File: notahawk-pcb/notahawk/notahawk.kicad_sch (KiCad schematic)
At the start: 33 parts, among them J1 Conn_01x02_Pin, U2 BNO085, U3 BMP581, U4 ADXL372BCCZ-RL7, U5 W25Q128JVSIQ, U6 ESP32-C3

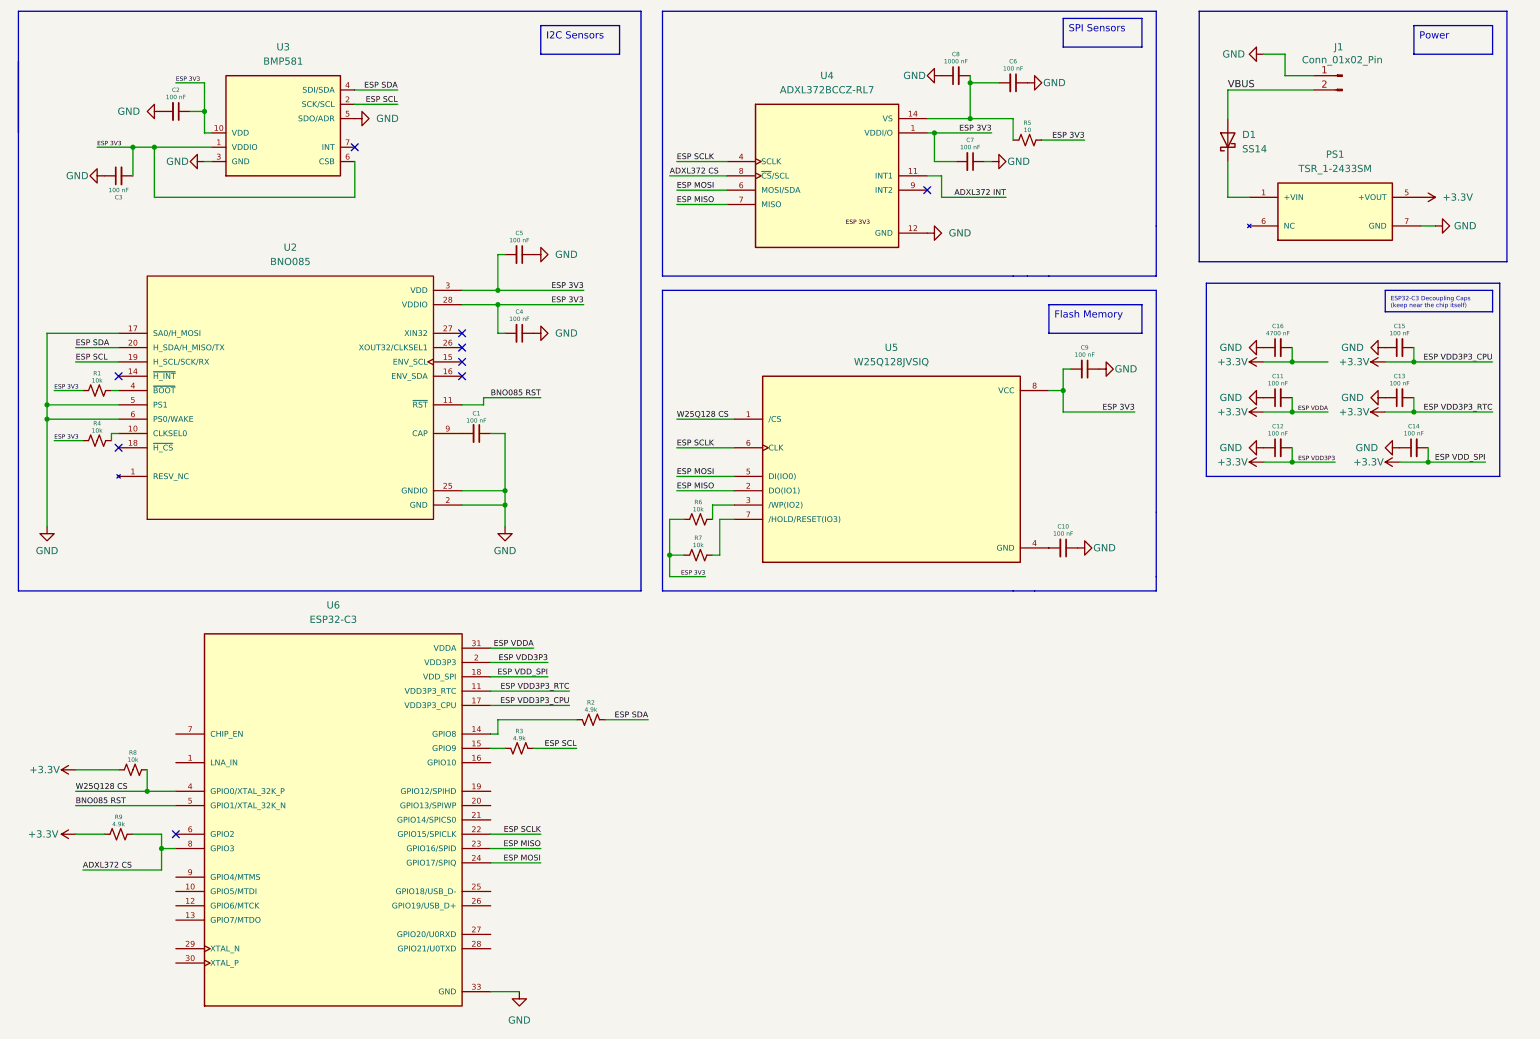
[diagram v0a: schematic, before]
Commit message: almost done w schematic
knocked off stuff from todo and then some. did circuit to handle boot/download/power modes

TODO:
- add QOL features to help debug board
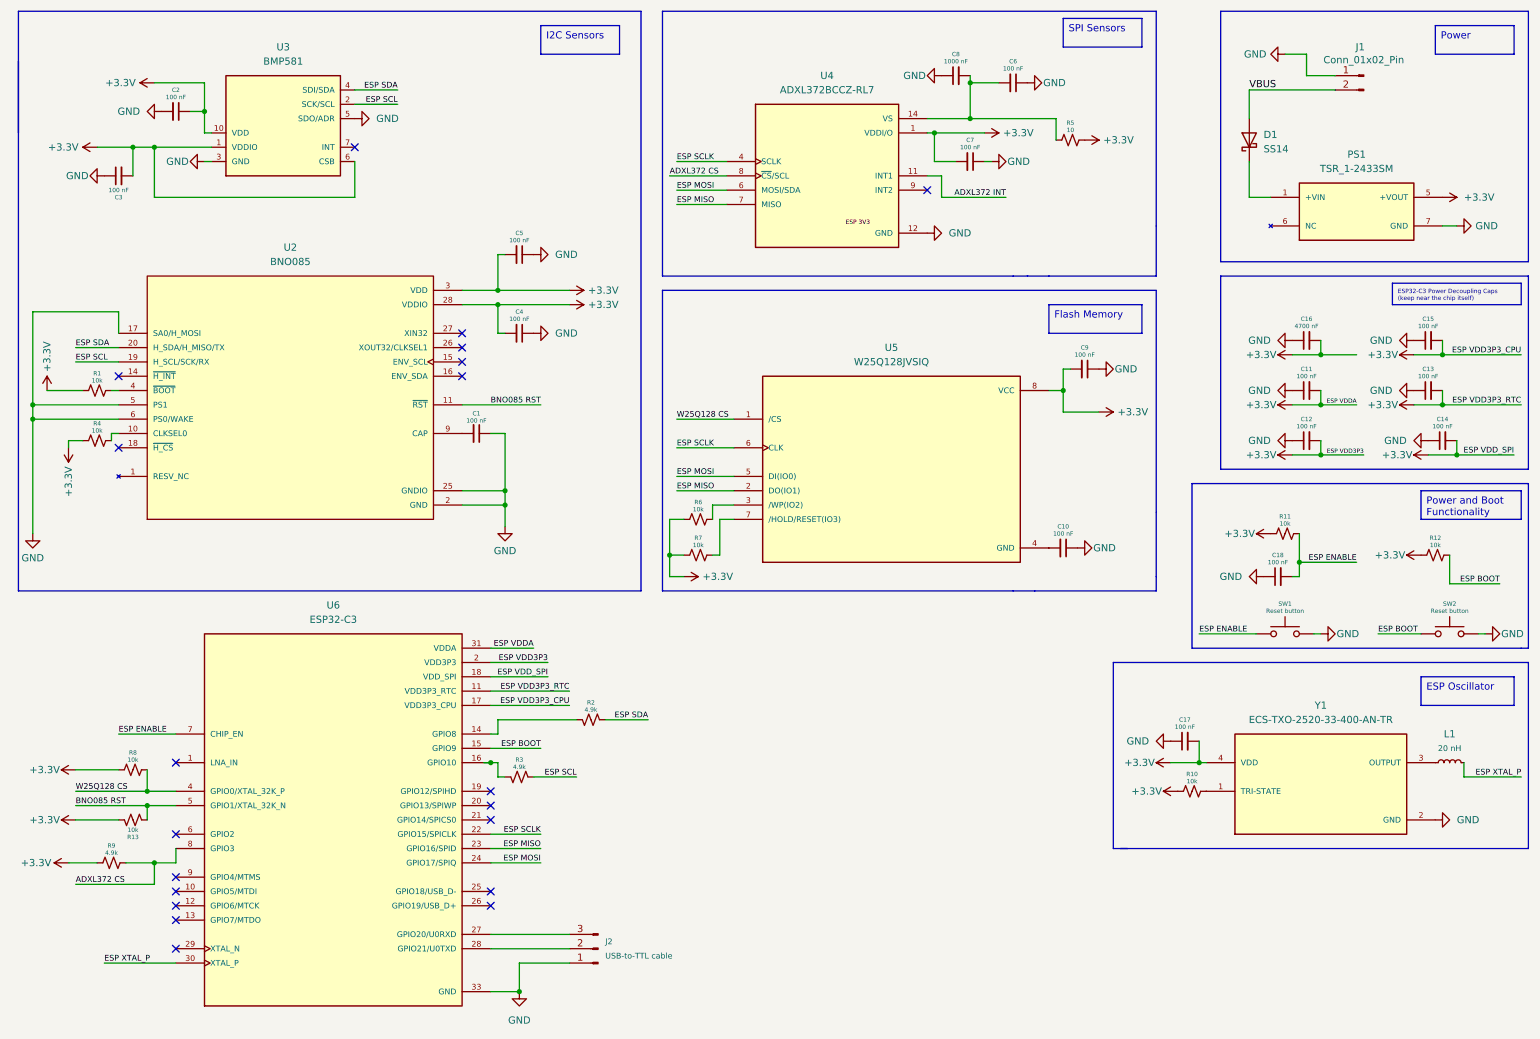
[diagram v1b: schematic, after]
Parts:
- added C17, C18: 100 nF, symbol Device:C_Small
- added J2: USB-to-TTL cable, symbol Connector:Conn_01x03_Pin
- added L1: 20 nH, symbol Device:L_Small
- added R10, R11, R12, R13: 10k, symbol Device:R_Small_US
- added SW1, SW2: Reset button, symbol Switch:SW_Push
- added Y1: ECS-TXO-2520-33-400-AN-TR, ECS-TXO-2520-33-400-AN-TR:OSC_ECS-TXO-2520-33-400-AN-TR, symbol crystals_additional:ECS-TXO-2520-33-400-AN-TR
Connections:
- net +3.3V: now also C2.1, C3.2, C4.2, C5.2, C7.2, C9.2, R1.2, R4.2, R5.1, R6.2, R7.2, U2.28 (VDDIO), U2.3 (VDD), U3.1 (VDDIO), U3.10 (VDD), U3.6 (CSB), U4.1 (VDDI/O), U5.8 (VCC), C17.2, R10.2, R11.2, R12.2, R13.2, Y1.4 (VDD)
- net ESP 3V3: no longer C2.1, C3.2, C4.2, C5.2, C7.2, C9.2, R1.2, R4.2, R5.1, R6.2, R7.2, U2.28 (VDDIO), U2.3 (VDD), U3.1 (VDDIO), U3.10 (VDD), U3.6 (CSB), U4.1 (VDDI/O), U5.8 (VCC)
- net GND: now also C17.1, C18.1, J2.1 (Pin_1), SW1.2, SW2.2, Y1.2 (GND)
- net at R3.1: now also U6.16 (GPIO10); no longer U6.15 (GPIO9)
- net at U6.27 (GPIO20/U0RXD): now also J2.3 (Pin_3)
- net at U6.28 (GPIO21/U0TXD): now also J2.2 (Pin_2)
- net ESP XTAL_P: now reaches U6.30 (XTAL_P)
- net ESP XTAL_P: now also L1.2
- net ESP ENABLE: now reaches U6.7 (CHIP_EN)
- net ESP ENABLE: now also C18.2, R11.1, SW1.1
- new net: R10.1, Y1.1 (TRI-STATE)
- new net: L1.1, Y1.3 (OUTPUT)
- new net ESP BOOT: R12.1, SW2.1, U6.15 (GPIO9)
- no-connect marks 9 -> 20
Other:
- moved on the sheet: C11, C12, C13, C14, C15, C16, D1, J1, PS1, R3, R5, R9

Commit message: finished schematic
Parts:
- added D2: POWER LED, symbol Device:LED
- added D3: BOOTLOADER LED, symbol Device:LED
- added D4: STATUS LED, symbol Device:LED
- added R14, R15: 1k, symbol Device:R_Small_US
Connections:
- net +3.3V: now also D2.2 (A), R14.1
- net ESP BOOT: now also D3.1 (K)
- net GND: now also D2.1 (K), D4.1 (K)
- net ESP STATUS: now reaches U6.26 (GPIO19/USB_D+)
- net ESP STATUS: now also R15.1
- new net: D3.2 (A), R14.2
- new net: D4.2 (A), R15.2
- no-connect marks 20 -> 19
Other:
- moved on the sheet: R12

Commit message: tiny changes
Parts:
- R5: value 10 -> 10 nF
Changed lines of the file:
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@@
 		)
 	)
-	(label "ESP 3V3"
-		(at 166.37 53.34 180)
-		(effects
-			(font
-				(size 0.762 0.762)
-			)
-			(justify right bottom)
-		)
-	)
 	(label "ESP VDD_SPI"
 		(at 280.67 93.98 180)
@@
 			)
 		)
-		(property "Value" "10"
+		(property "Value" "10 nF"
 			(at 201.93 36.322 90)
 			(effects

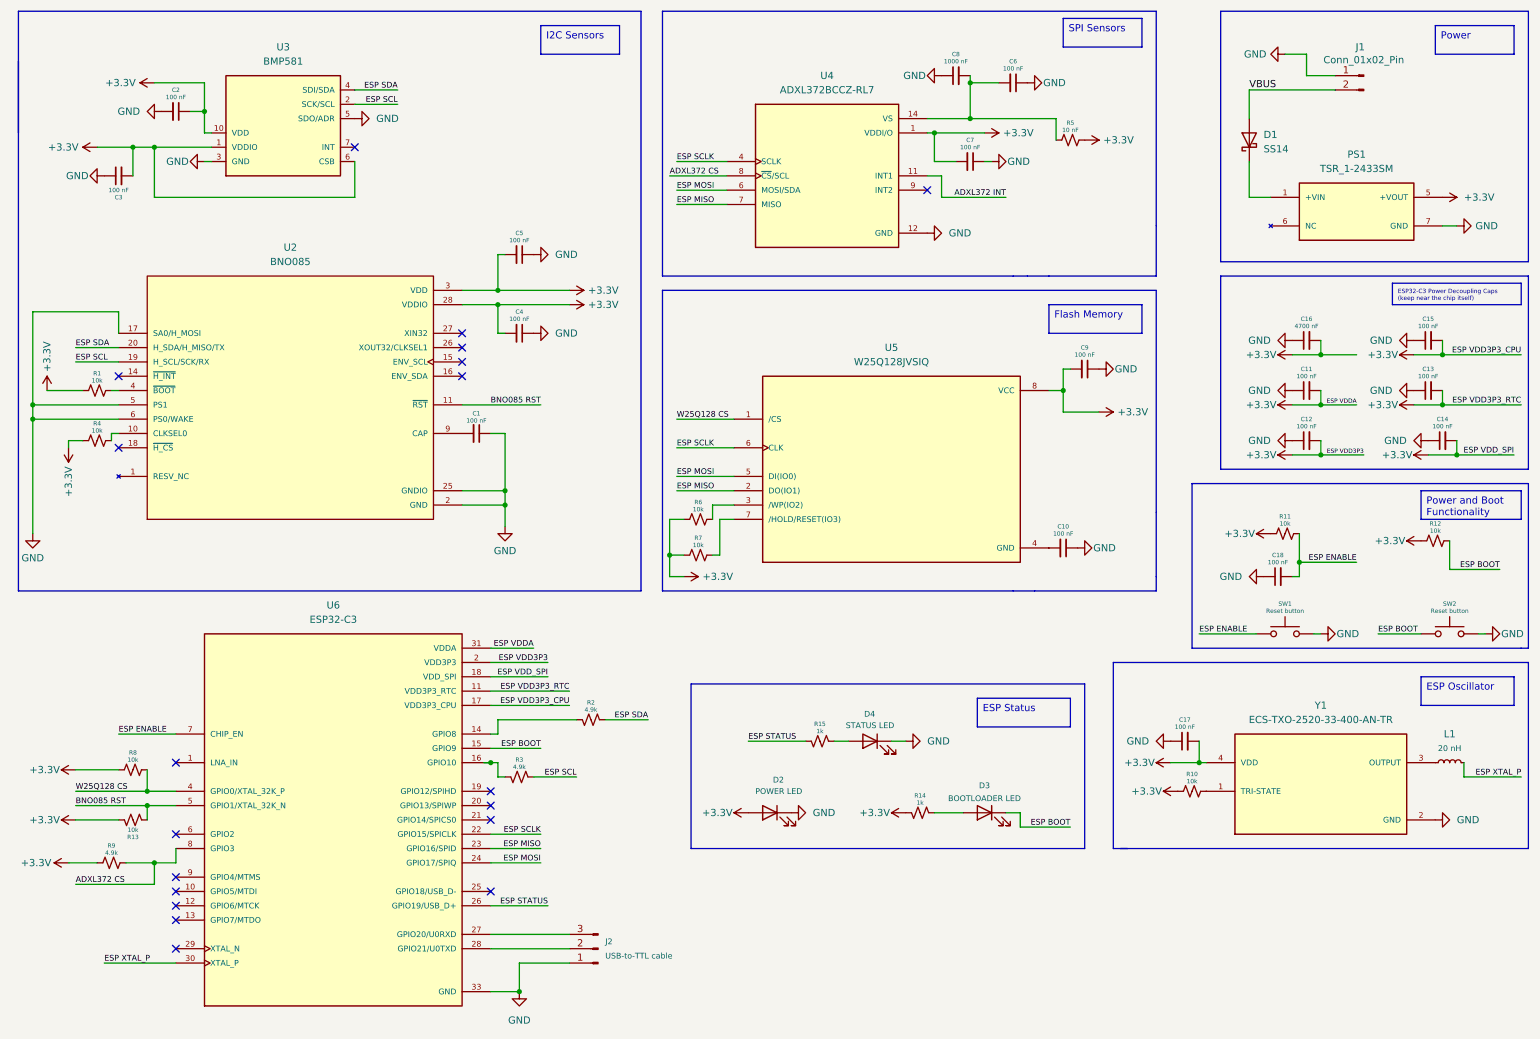
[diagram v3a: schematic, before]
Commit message: fixed erc errors on schematic
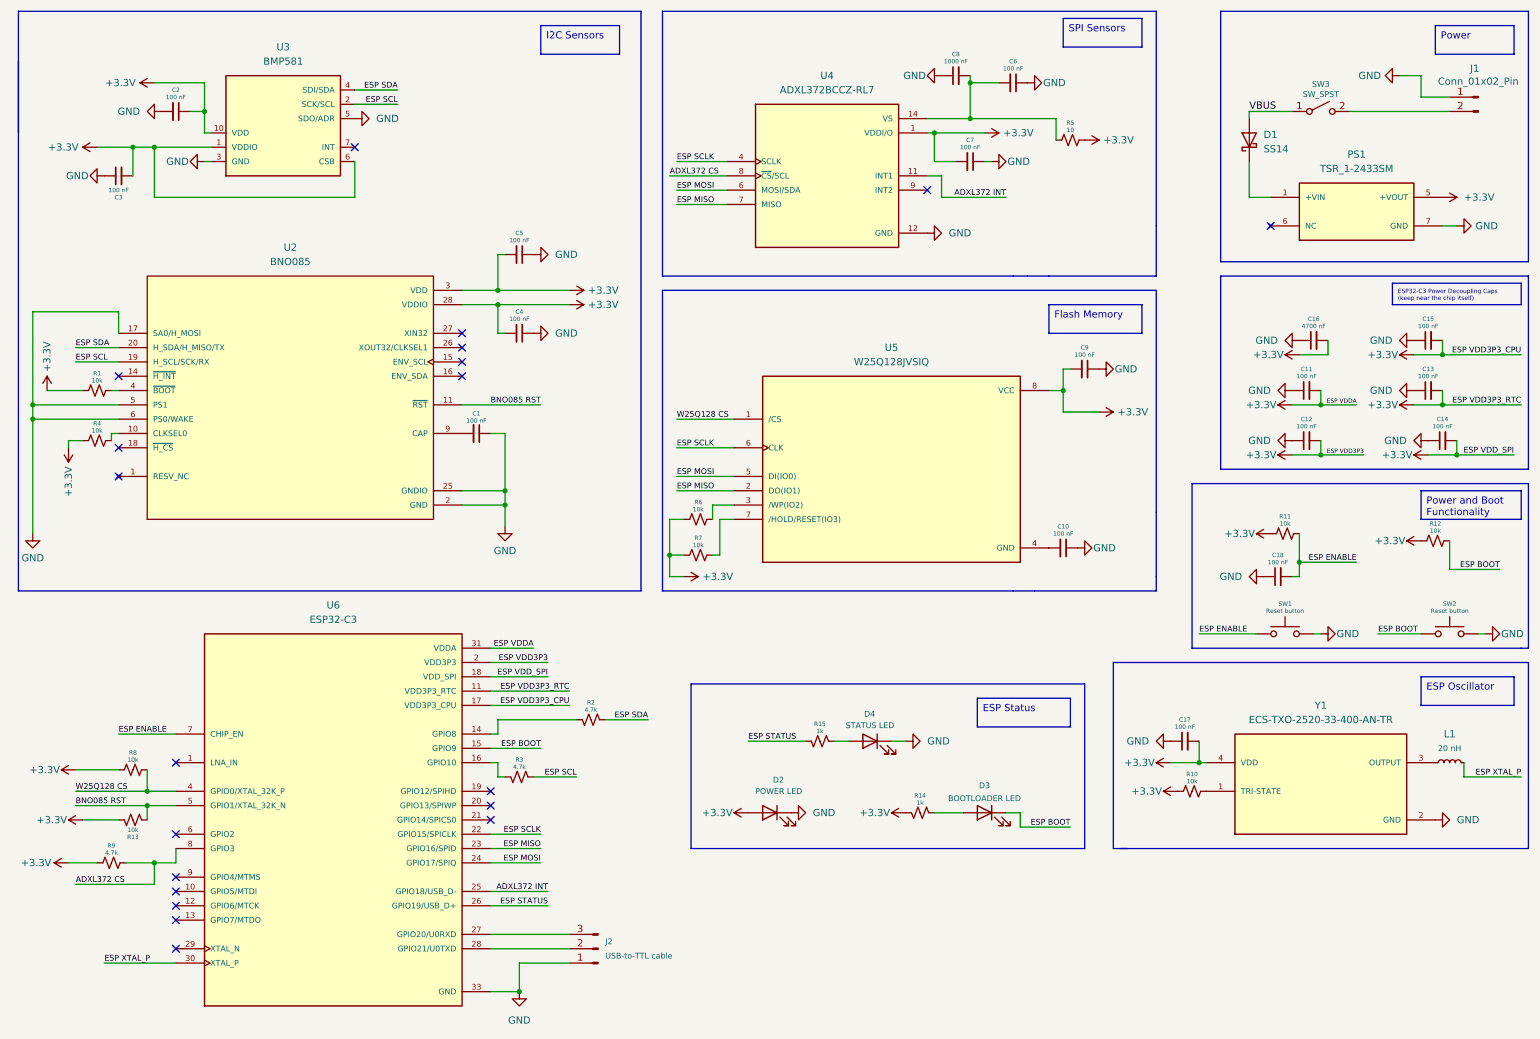
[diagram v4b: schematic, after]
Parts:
- added SW3: SW_SPST, burner:SW_DS04-254-2-01BK-SMT, symbol Switch:SW_SPST
- J1: footprint (none) -> Connector_PinSocket_2.54mm:PinSocket_1x02_P2.54mm_Vertical_SMD_Pin1Left
- J2: footprint (none) -> Connector_PinSocket_2.54mm:PinSocket_1x03_P2.54mm_Vertical
- L1: footprint (none) -> burner:INDC1005X55N
- R2, R3, R9: value 4.9k -> 4.7k
- R5: value 10 nF -> 10
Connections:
- net ADXL372 INT: now also U6.25 (GPIO18/USB_D-)
- net BNO085 RST: now also R13.1
- net VBUS: now also SW3.1 (A); no longer J1.2 (Pin_2)
- new net: J1.2 (Pin_2), SW3.2 (B)
- no-connect marks 19 -> 20
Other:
- moved on the sheet: C16, J1

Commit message: mo footprints
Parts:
- L1: footprint burner:INDC1005X55N -> inductor_additional:INDC1005X55N
- SW3: footprint burner:SW_DS04-254-2-01BK-SMT -> switches_additional:SW_DS04-254-2-01BK-SMT
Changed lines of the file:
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@@
 			)
 		)
-		(property "Footprint" "burner:SW_DS04-254-2-01BK-SMT"
+		(property "Footprint" "switches_additional:SW_DS04-254-2-01BK-SMT"
 			(at 246.38 33.02 0)
 			(effects
@@
 			)
 		)
-		(property "Footprint" "burner:INDC1005X55N"
+		(property "Footprint" "inductor_additional:INDC1005X55N"
 			(at 269.24 148.59 0)
 			(effects
